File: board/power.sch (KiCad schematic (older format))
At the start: 97 parts, among them P47 CONN_2, P48 CONN_2, U14 TPS53319, U3 TPS54625, U4 TPS54625, U5 TPS54625, U6 TPS51200

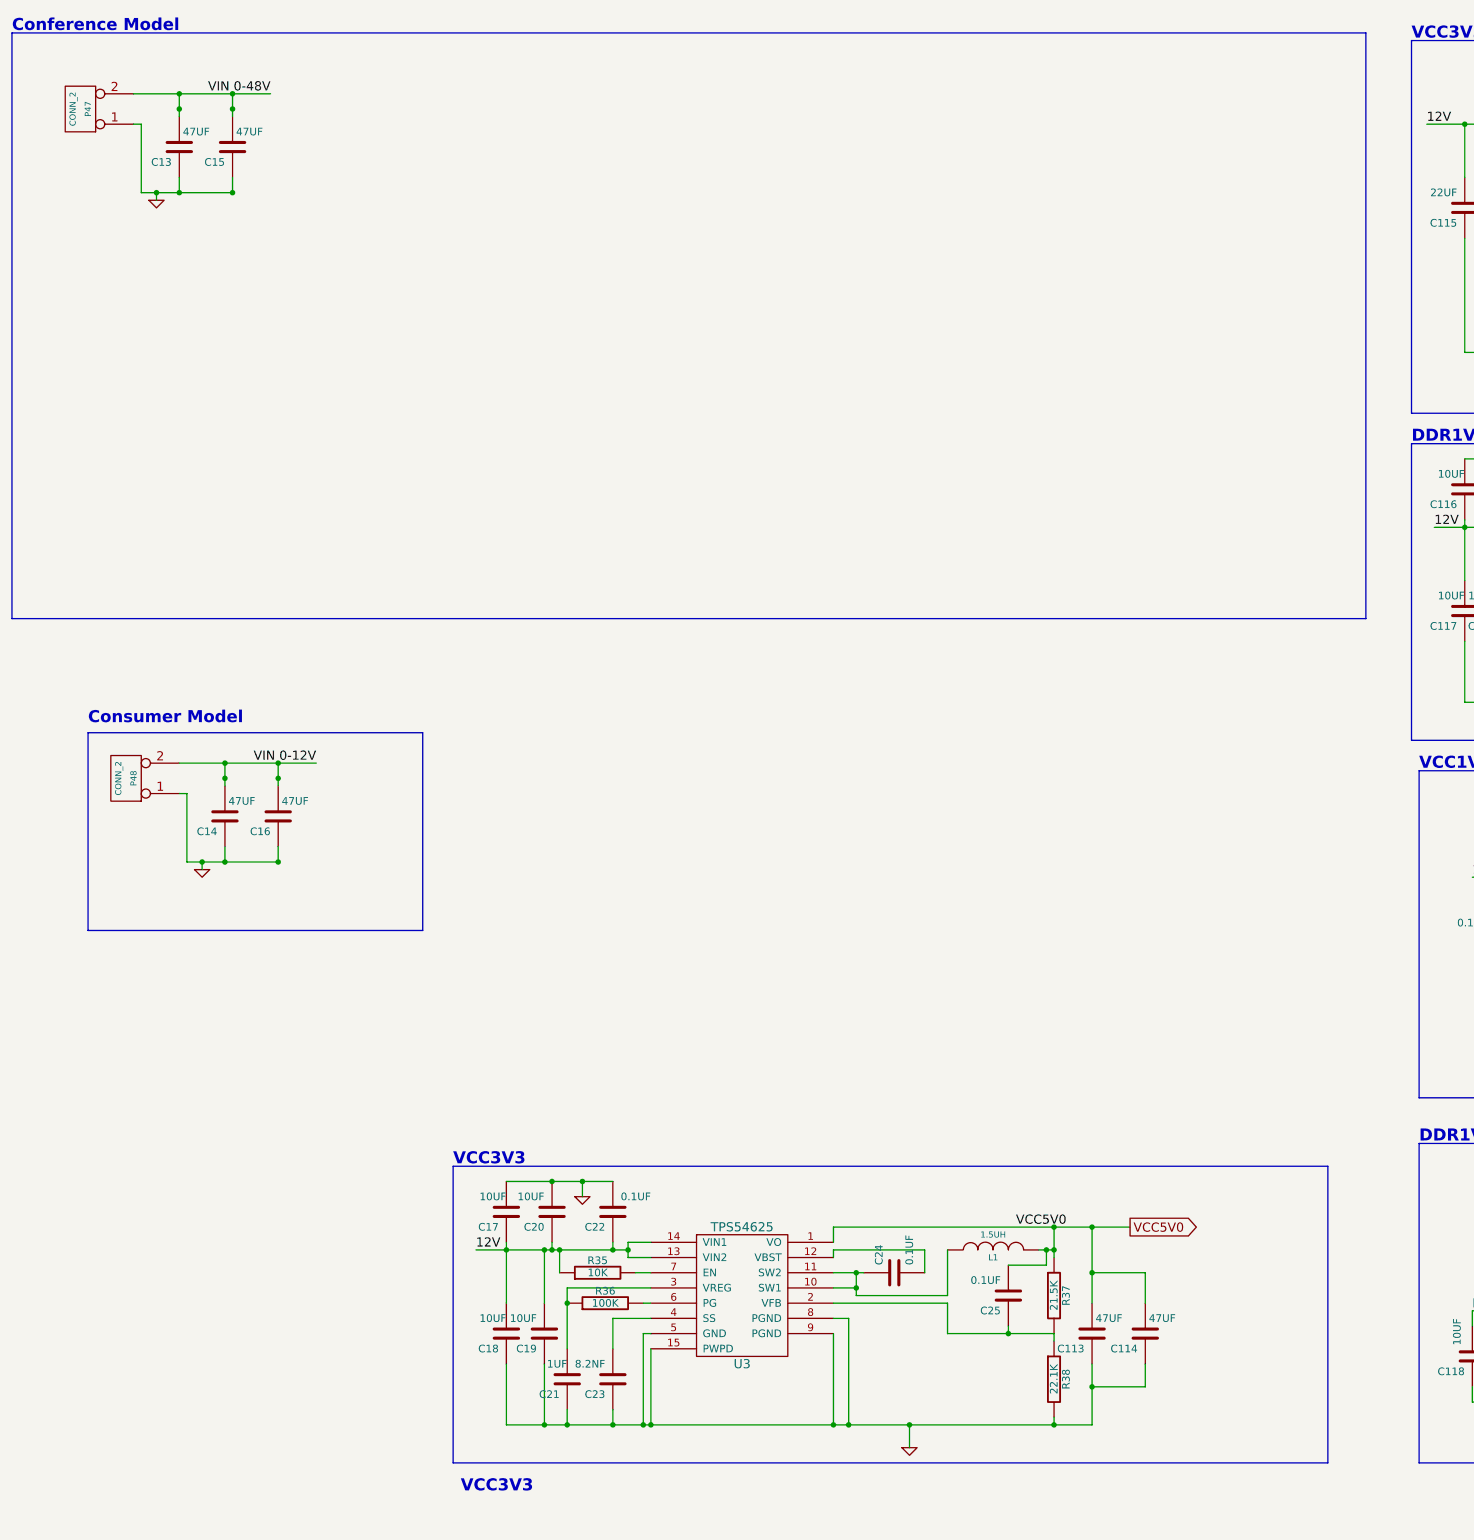
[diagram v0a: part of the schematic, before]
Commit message: Issue #958 - Power supply schematic completed
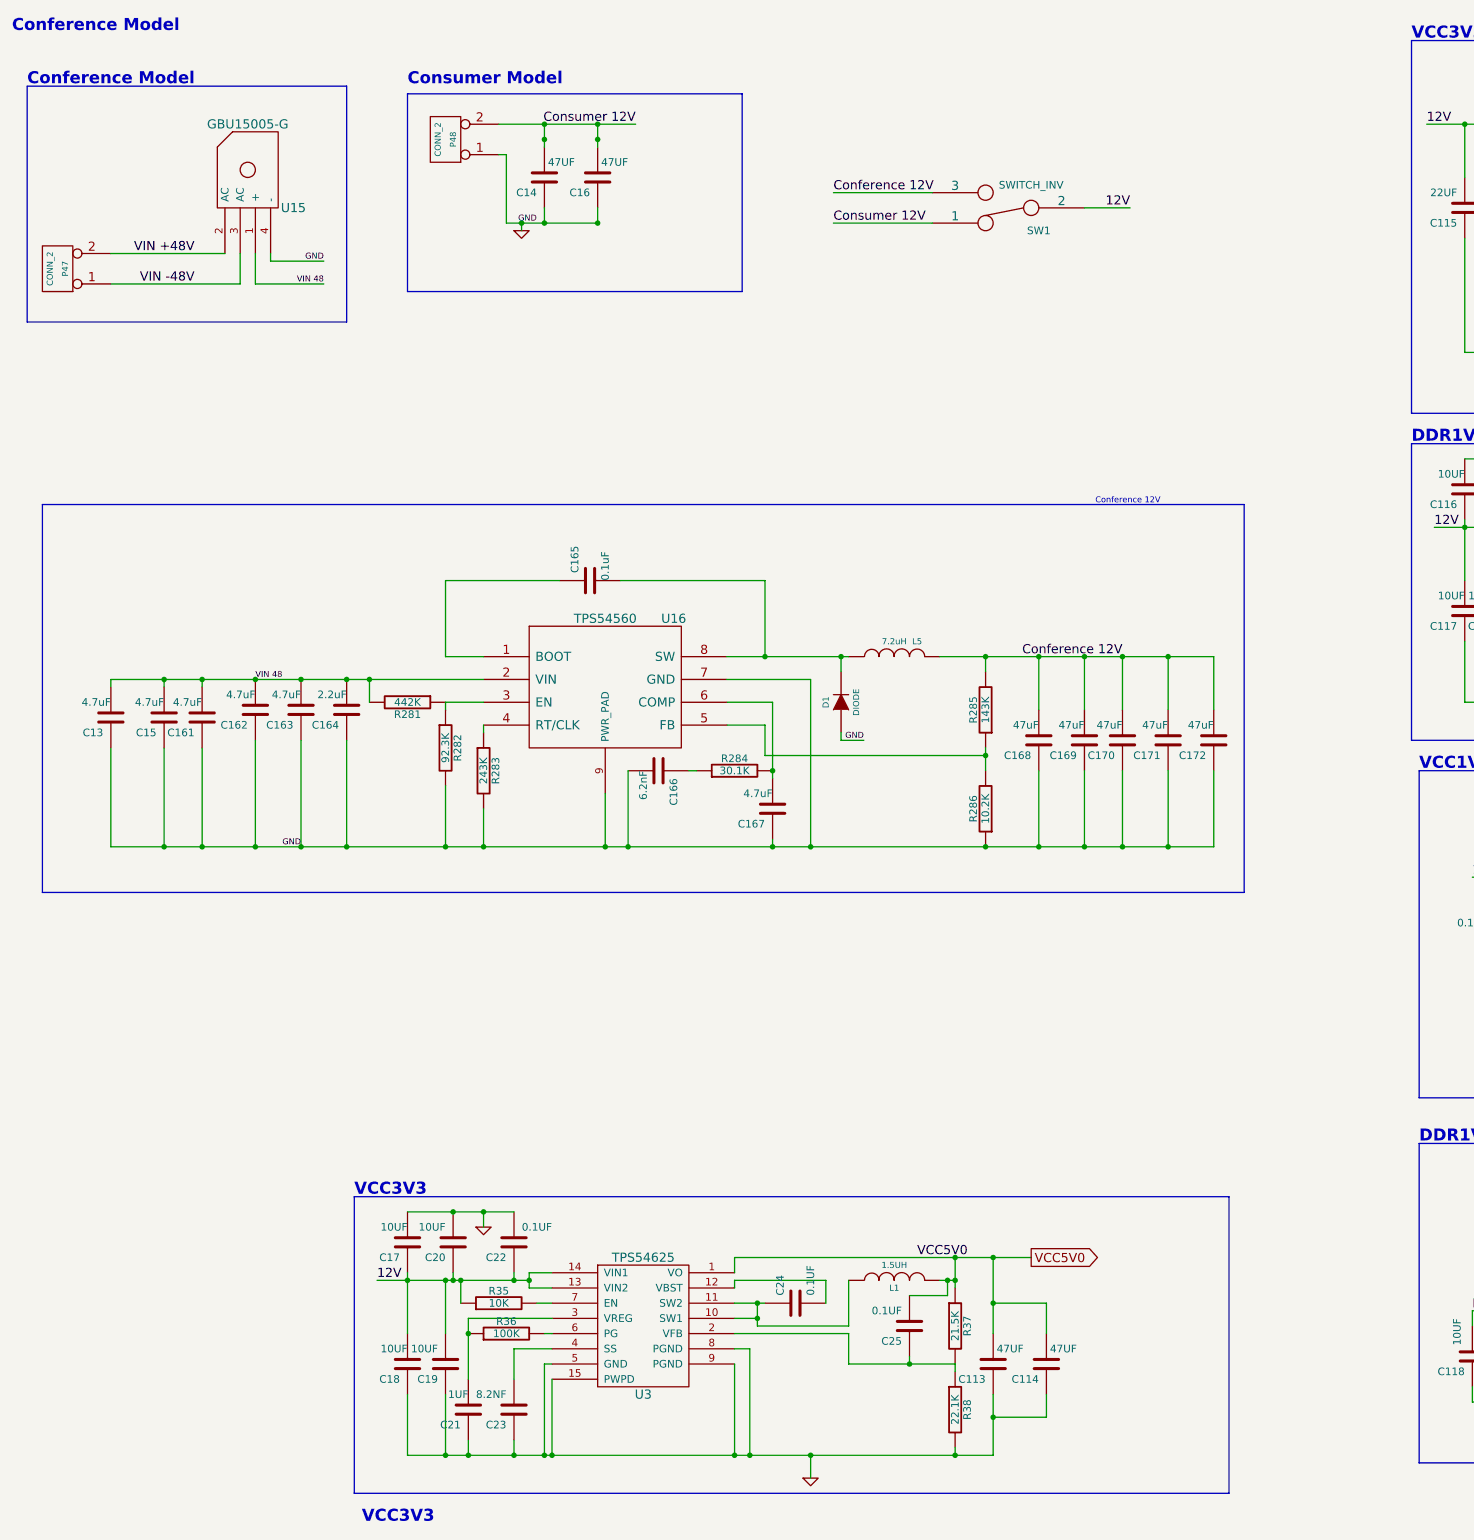
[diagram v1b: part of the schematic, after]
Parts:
- added C161, C162, C163, C167: 4.7uF, symbol C
- added C164: 2.2uF, symbol C
- added C165: 0.1uF, symbol C
- added C166: 6.2nF, symbol C
- added C168, C169, C170, C171, C172: 47uF, symbol C
- added D1: DIODE, ~, symbol DIODE
- added L5: 7.2uH, symbol INDUCTOR
- added R281: 442K, symbol R
- added R282: 92.3K, symbol R
- added R283: 243K, symbol R
- added R284: 30.1K, symbol R
- added R285: 143K, symbol R
- added R286: 10.2K, symbol R
- added SW1: SWITCH_INV, ~, symbol SWITCH_INV
- added U15: GBU15005-G, ~, symbol GBU15005-G
- added U16: TPS54560, ~, symbol TPS54560
- C13, C15: value 47UF -> 4.7uF
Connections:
- net 12V: now also SW1.2
- net GND: now also C161.1, C162.1, C163.1, C164.1, C166.2, C167.1, C168.1, C169.1, C170.1, C171.1, C172.1, D1.1 (A), R282.2, R283.2, R286.1, U15.4 (-), U16.7 (GND), U16.9 (PWR_PAD); no longer P47.1 (P1)
- net VIN  0-12V renamed Consumer 12V
- net Consumer 12V: now also SW1.1
- net VIN 0-48V renamed VIN 48
- net VIN 48: now also C161.2, C162.2, C163.2, C164.2, R281.2, U15.1 (+), U16.2 (VIN); no longer P47.2 (PM)
- new net: C165.1, U16.1 (BOOT)
- new net: R281.1, R282.1, U16.3 (EN)
- new net: R283.1, U16.4 (RT/CLK)
- new net: R285.1, R286.2, U16.5 (FB)
- new net: C167.2, R284.2, U16.6 (COMP)
- new net: C165.2, D1.2 (K), L5.1, U16.8 (SW)
- new net: C166.1, R284.1
- new net Conference 12V: C168.2, C169.2, C170.2, C171.2, C172.2, L5.2, R285.2, SW1.3
- new net VIN +48V: P47.2 (PM), U15.2 (AC)
- new net VIN -48V: P47.1 (P1), U15.3 (AC)
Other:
- note added: "Conference 12V"
- moved on the sheet: C113, C114, C14, C16, C17, C18, C19, C20, C21, C22, C23, C24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

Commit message: Issue #921 - vhdci routing
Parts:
- added R? (x12): 0.2E 2W, symbol R
- added R? (x12): 10K, symbol R
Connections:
- net DDR0V9: now also R?.1, R?.1, R?.2; no longer C146.2, C148.2, C152.2, C155.2, C158.2, U6.3 (VO), U6.5 (VOSNS)
- net DDR1V8: now also R?.1, R?.1, R?.2, R?.2, R?.2
- net GND: now also R?.1, R?.1, R?.1, R?.1, R?.1, R?.1; no longer C113.1, C114.1, C18.1, C19.1, C21.1, C23.1, R38.2, U3.15 (PWPD), U3.5 (GND), U3.8 (PGND), U3.9 (PGND)
- net VCC1V2: now also R?.1, R?.1, R?.1, R?.1, R?.2, R?.2; no longer C147.1, C154.2, C156.2, L3.2, R277.1, U5.1 (VO)
- net VCC3V3: now also R?.1, R?.1, R?.2; no longer C151.1, C157.2, C159.2, C160.2, L4.2, R279.2
- net 12V renamed VCC12V0
- net VCC12V0: no longer SW1.2
- net VCC5V0 renamed VCC5V0_RS+
- net VCC5V0_RS+: now also C147.1, C154.2, C156.2, L3.2, R277.1, U5.1 (VO), R?.2, R?.2, R?.2, R?.2
- new net: C113.1, C114.1, C18.1, C19.1, C21.1, C23.1, R38.2, U3.15 (PWPD), U3.5 (GND), U3.8 (PGND), U3.9 (PGND)
- new net DDR0V9_RS+: C146.2, C148.2, C152.2, C155.2, C158.2, R?.2, R?.2, U6.3 (VO), U6.5 (VOSNS)
- new net DDR3V3_RS+: C151.1, C157.2, C159.2, C160.2, L4.2, R279.2, R?.2, R?.2
- new net PICADC0: R?.1, R?.2
- new net PICADC1: R?.1, R?.2
- new net PICADC2: R?.1, R?.2
- new net PICADC3: R?.1, R?.2
- new net PICADC4: R?.1, R?.2
- new net PICADC5: R?.1, R?.2
- new net VCC12V0_RS+: R?.2, R?.2, SW1.2
- new net VCC12V0_RS-: R?.1, R?.1, R?.2
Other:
- note added: "DDR0V9"
- note added: "VCC5V0"
- moved on the sheet: C113, C114, C115, C116, C117, C118, C119, C120, C121, C122, C123, C124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

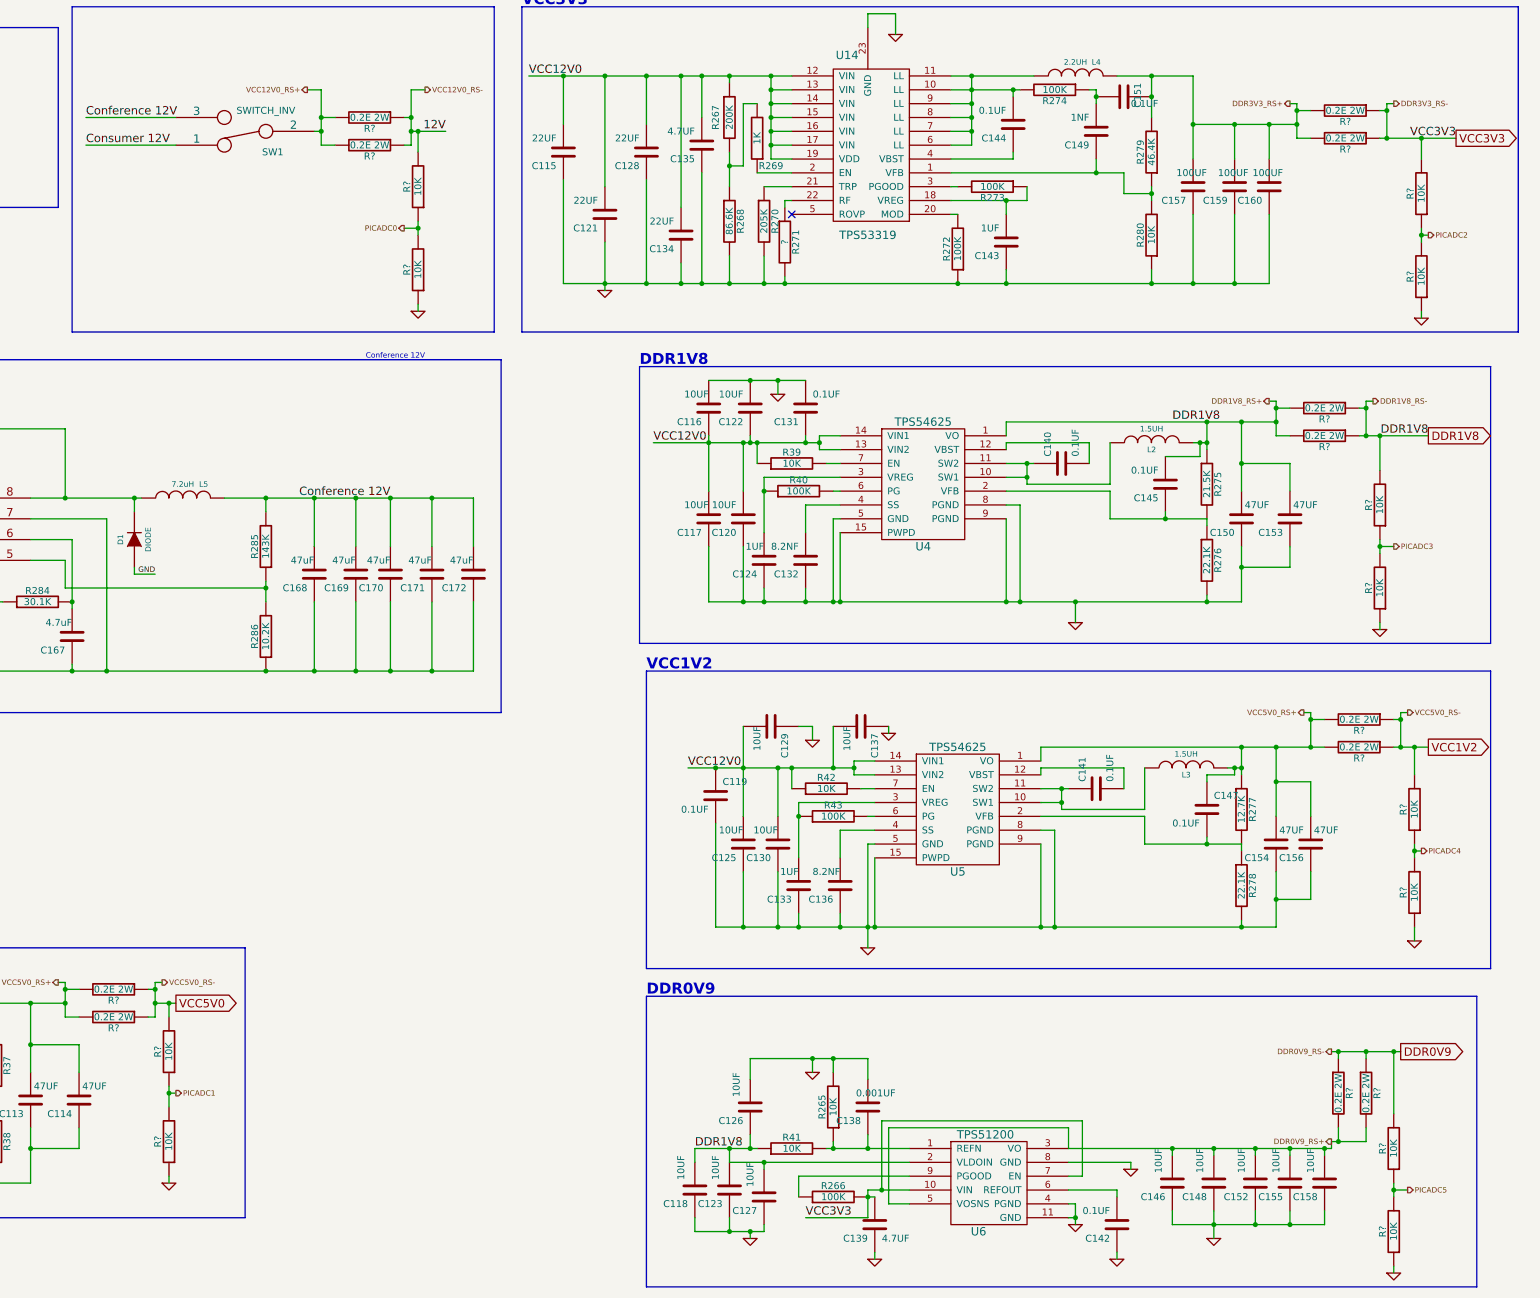
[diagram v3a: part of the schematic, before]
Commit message: Issue #934 - GTP routing
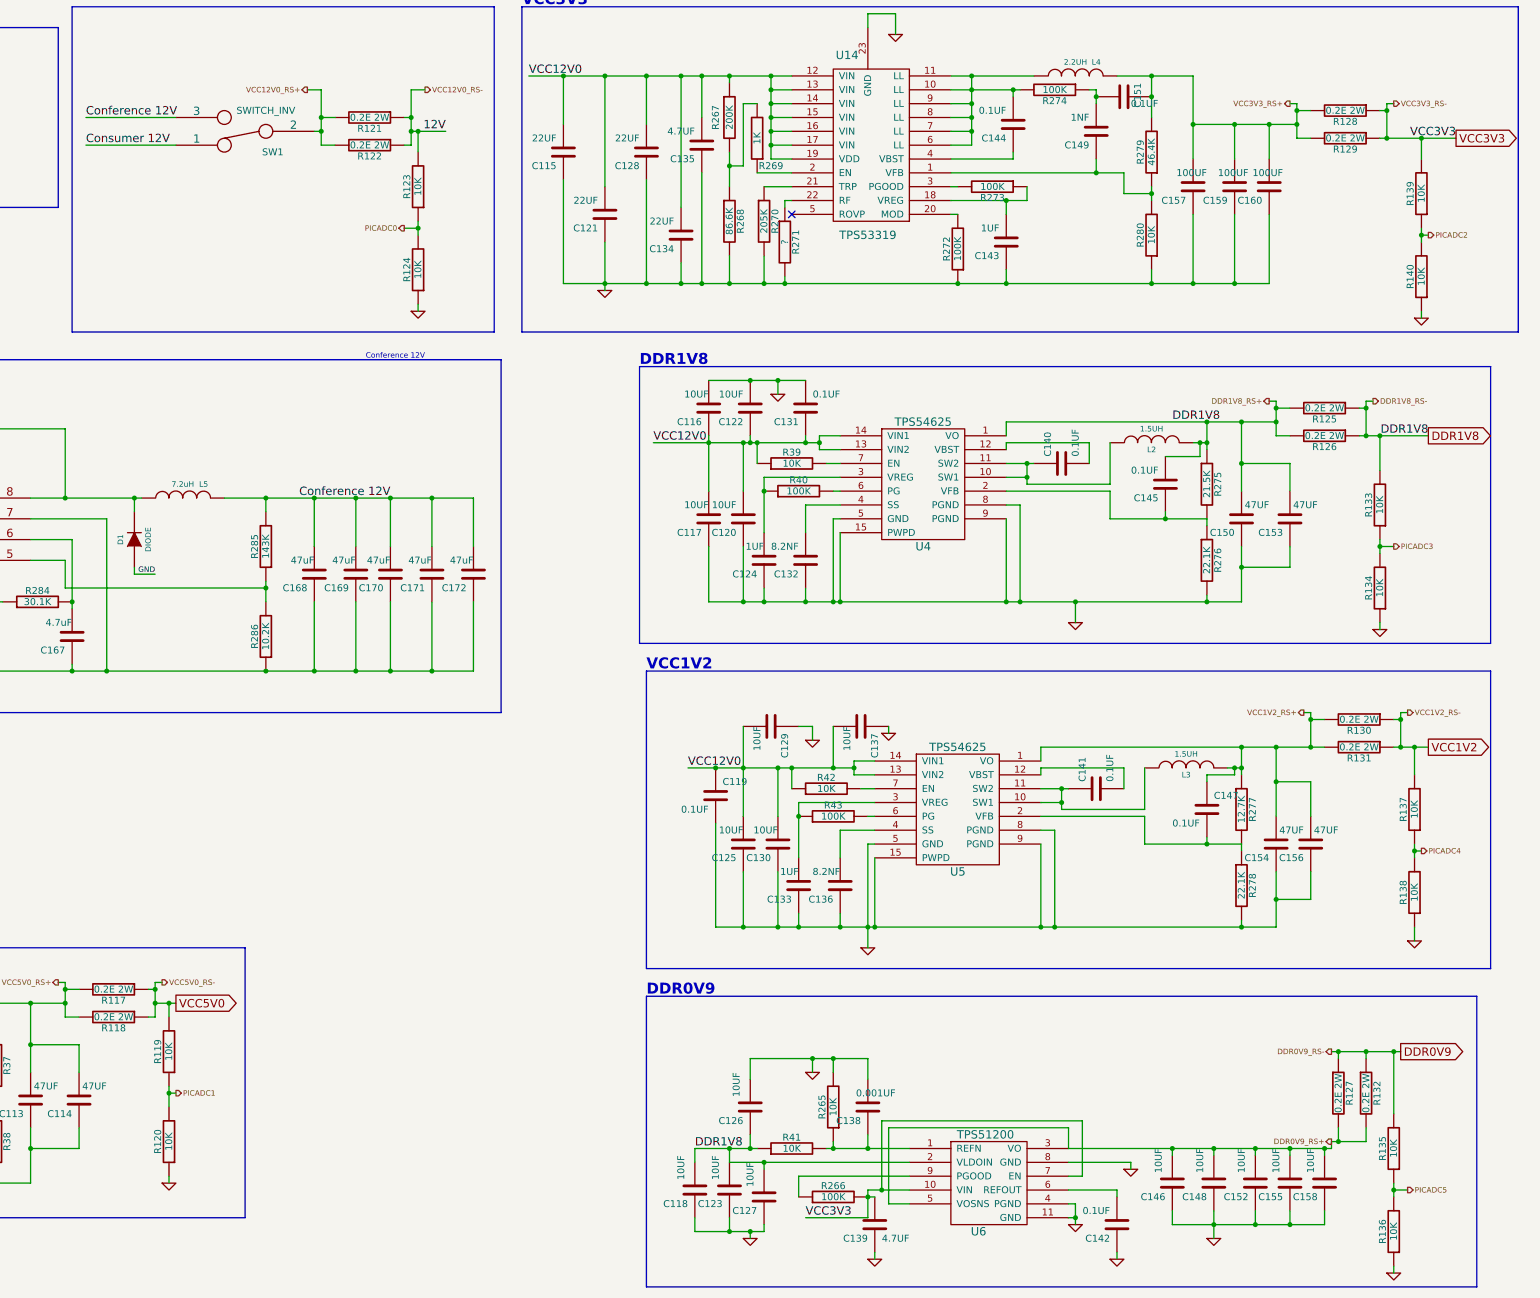
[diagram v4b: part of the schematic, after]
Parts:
- gave numbers to parts that had none: 24
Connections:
- net VCC1V2: no longer R117.1, R118.1, R119.2
- net VCC5V0_RS+: no longer C147.1, C154.2, C156.2, L3.2, R130.2, R131.2, R277.1, U5.1 (VO)
- net DDR3V3_RS+ renamed VCC3V3_RS+
- new net VCC1V2_RS+: C147.1, C154.2, C156.2, L3.2, R130.2, R131.2, R277.1, U5.1 (VO)
- new net VCC5V0: R117.1, R118.1, R119.2
